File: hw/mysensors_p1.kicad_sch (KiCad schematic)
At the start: 8 parts, among them J1 RJ12, J2 Conn_01x06_Socket, U2 NRF24L01_Breakout

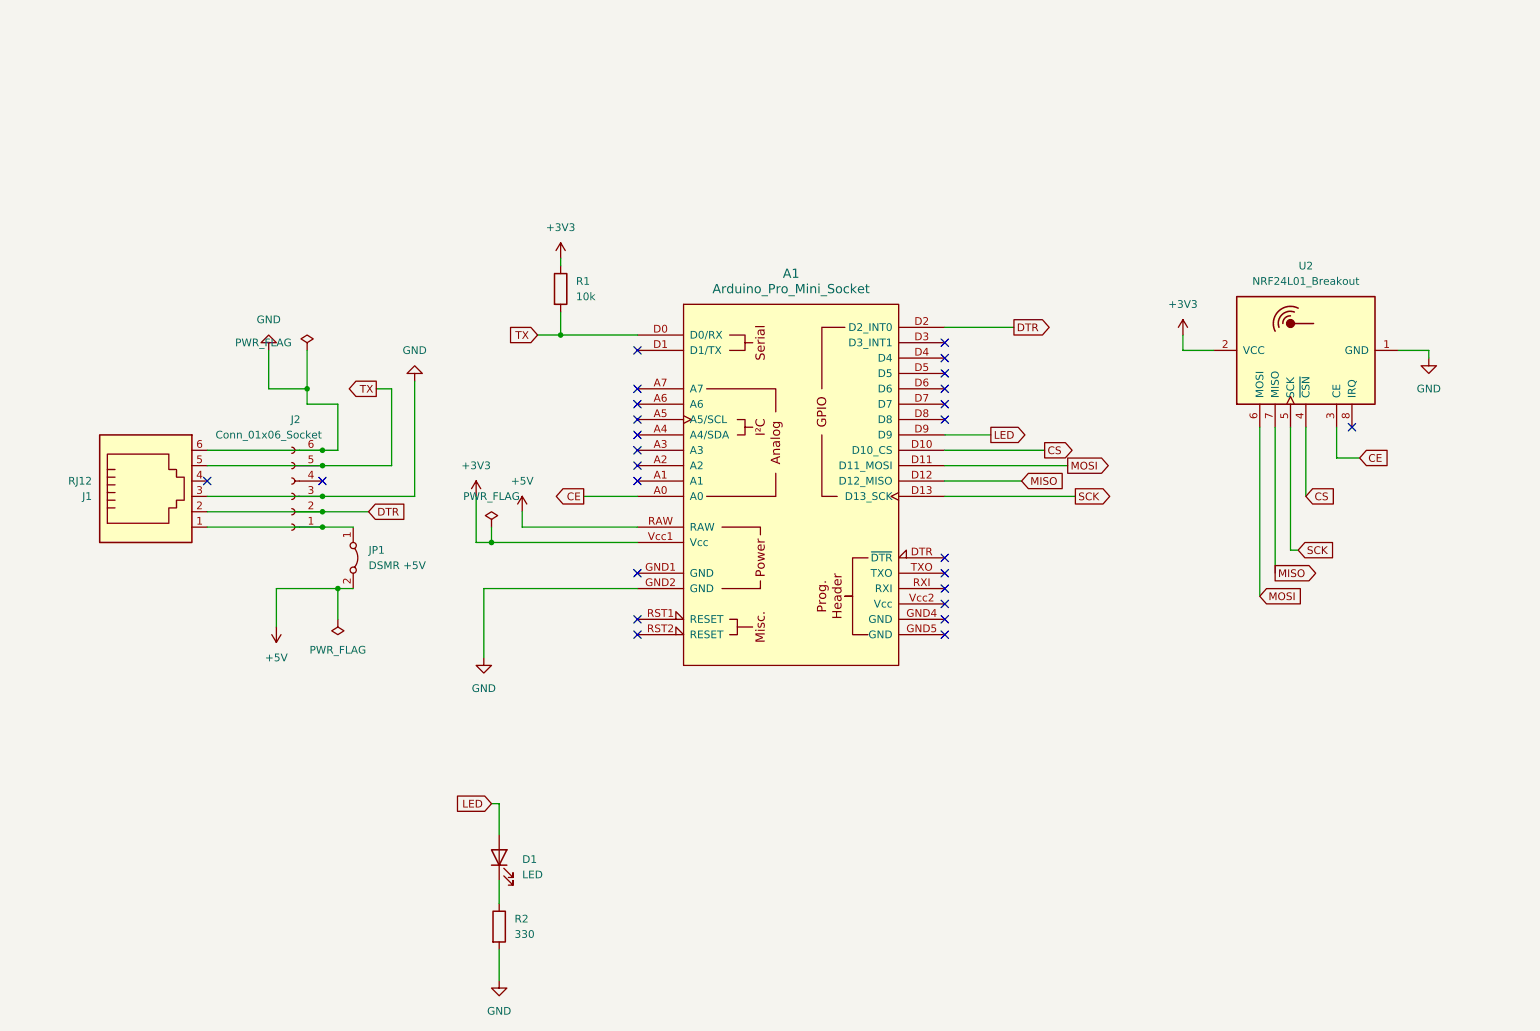
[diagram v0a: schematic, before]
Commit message: More or less working, just electricity power for now.
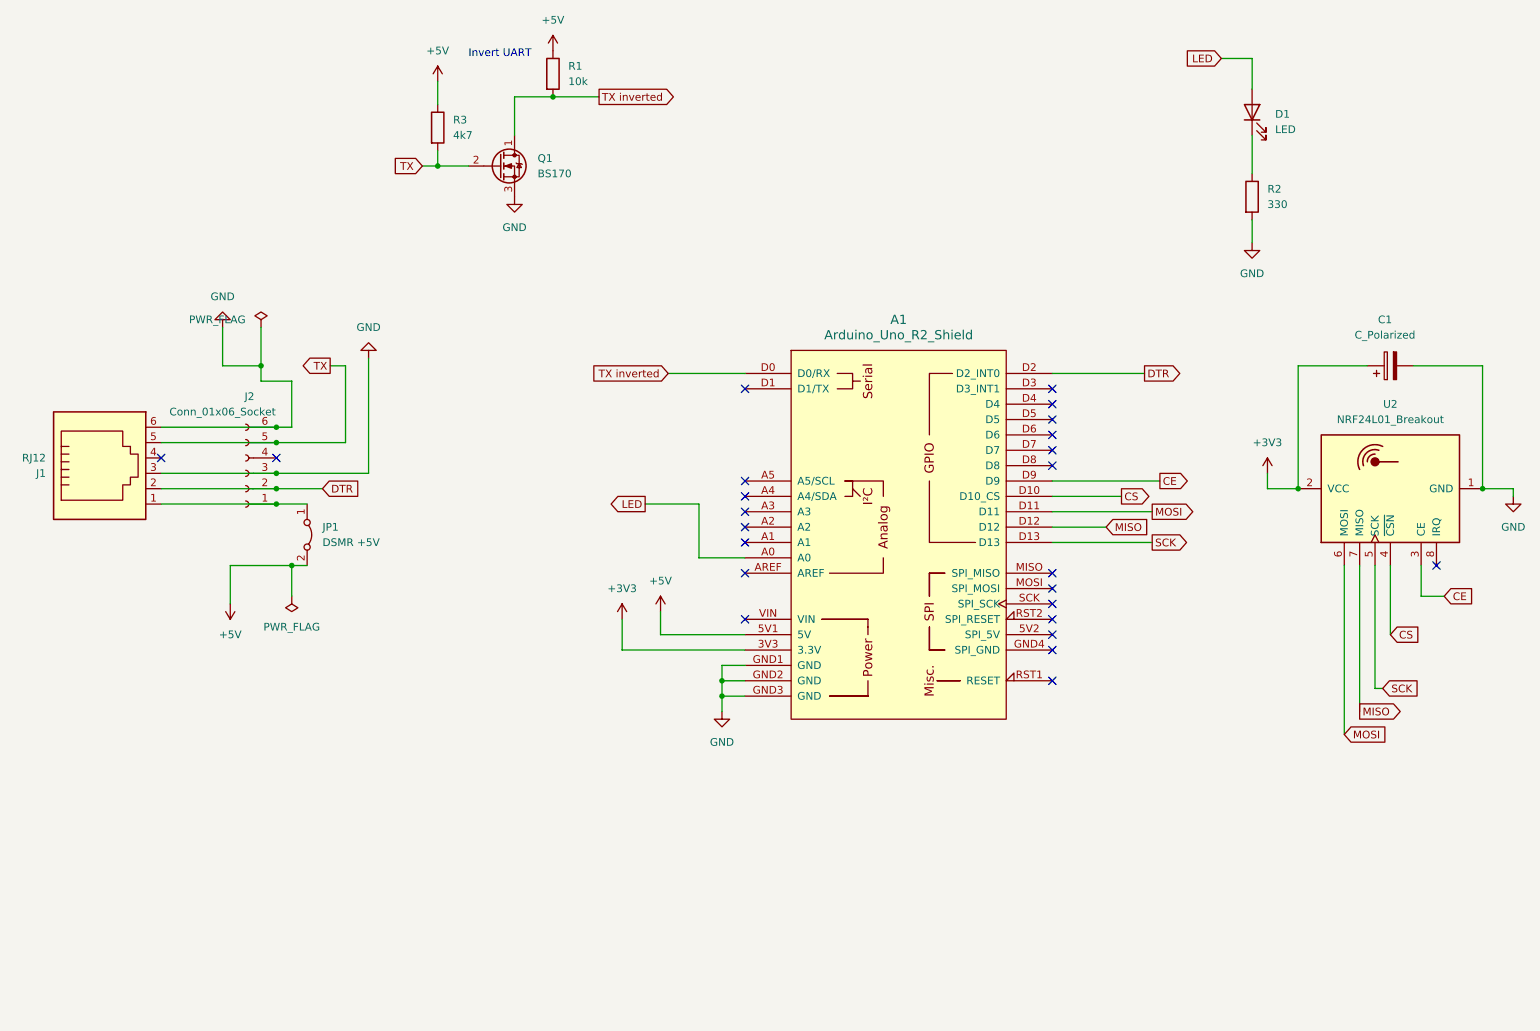
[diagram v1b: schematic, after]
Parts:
- removed A1: Arduino_Pro_Mini_Socket, PCM_arduino-library:Arduino_Pro_Mini_Socket, symbol PCM_arduino-library:Arduino_Pro_Mini_Socket
- added A1: Arduino_Uno_R2_Shield, PCM_arduino-library:Arduino_Uno_R2_Shield, symbol PCM_arduino-library:Arduino_Uno_R2_Shield
- added C1: C_Polarized, symbol Device:C_Polarized
- added Q1: BS170, Package_TO_SOT_THT:TO-92_Inline, symbol Transistor_FET:BS170
- added R3: 4k7, Resistor_THT:R_Axial_DIN0207_L6.3mm_D2.5mm_P10.16mm_Horizontal, symbol Device:R
- D1: footprint LED_THT:LED_D3.0mm -> LED_THT:LED_D5.0mm
- R2: footprint Resistor_THT:R_Axial_DIN0207_L6.3mm_D2.5mm_P10.16mm_Horizontal -> Resistor_THT:R_Axial_DIN0207_L6.3mm_D2.5mm_P2.54mm_Vertical
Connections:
- net +3V3: now also A1.3V3 (3.3V), C1.1; no longer R1.1
- net +5V: now also R1.1, A1.5V1 (5V), R3.1
- net CE: now also A1.D9
- net CS: now also A1.D10 (D10_CS)
- net DTR: now also A1.D2 (D2_INT0)
- net GND: now also A1.GND1 (GND), A1.GND2 (GND), A1.GND3 (GND), C1.2, Q1.3 (S)
- net LED: now also A1.A0
- net MISO: now also A1.D12
- net MOSI: now also A1.D11
- net SCK: now also A1.D13
- net TX: now also Q1.2 (G), R3.2; no longer R1.2
- new net TX inverted: A1.D0 (D0/RX), Q1.1 (D), R1.2
- no-connect marks 26 -> 24
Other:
- note added: "Invert UART"
- moved on the sheet: J1, J2, JP1, R1, U2
